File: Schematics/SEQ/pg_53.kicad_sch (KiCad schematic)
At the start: 6 parts, among them U5401 F30, U5402 F148, U5403 F02, U5404 F20, U5405 F240, U5406 F374

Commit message: Much SEQ polishing
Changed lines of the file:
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@@
   (bus (pts (xy 487.68 193.04) (xy 487.68 198.12) ) (stroke (width 0) (type solid) (color 0 0 0 0) ) )
   (bus (pts (xy 487.68 198.12) (xy 487.68 203.2) ) (stroke (width 0) (type solid) (color 0 0 0 0) ) )
-  (bus (pts (xy 487.68 203.2) (xy 487.68 210.82) ) (stroke (width 0) (type solid) (color 0 0 0 0) ) )
   (bus (pts (xy 487.68 93.98) (xy 487.68 99.06) ) (stroke (width 0) (type solid) (color 0 0 0 0) ) )
   (bus (pts (xy 487.68 93.98) (xy 497.84 93.98) ) (stroke (width 0) (type solid) (color 0 0 0 0) ) )

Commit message: KiCad 6
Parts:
- U5401: value F30 -> (none)
- U5402: value F148 -> (none)
- U5403: value F02 -> (none)
- U5404: value F20 -> (none)
- U5405: value F240 -> (none)
- U5406: value F374 -> (none)

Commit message: Recover from KiCad-6 munging
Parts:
- U5401: value (none) -> F30
- U5402: value (none) -> F148
- U5403: value (none) -> F02
- U5404: value (none) -> F20
- U5405: value (none) -> F240
- U5406: value (none) -> F374

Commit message: Megacompification
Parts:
- removed U5403: F02, symbol r1000:F02
- removed U5405: F240, symbol r1000:F240
- U5406: value F374 -> XREG14; symbol r1000:F374 -> r1000:XREG14; Location N17 -> x99; Name LMUAD1 -> LMUAD
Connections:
- net L_MACRO_HIC~: now also U5406.3 (OE); no longer U5406.1 (OE)
- net PD: now also U5406.16 (D5), U5406.20 (D7); no longer U5406.4 (D1)
- net PU: now also U5406.10 (D2), U5406.12 (D3), U5406.28 (D11), U5406.30 (D12), U5406.32 (D13), U5406.6 (D0), U5406.8 (D1); no longer U5406.17 (D6), U5406.3 (D0)
- net UADR~0: now also U5406.7 (Q0)
- net UADR~1: now also U5406.9 (Q1)
- net UADR~10: now also U5406.27 (Q10); no longer U5406.12 (Q4)
- net UADR~11: now also U5406.29 (Q11); no longer U5406.15 (Q5)
- net UADR~12: now also U5406.31 (Q12); no longer U5406.16 (Q6)
- net UADR~13: now also U5406.33 (Q13); no longer U5406.19 (Q7)
- net UADR~2: now also U5406.11 (Q2)
- net UADR~3: now also U5406.13 (Q3)
- net UADR~4: now also U5406.15 (Q4)
- net UADR~5: now also U5406.17 (Q5)
- net UADR~6: now also U5406.19 (Q6); no longer U5406.2 (Q0)
- net UADR~7: now also U5406.21 (Q7); no longer U5406.5 (Q1)
- net UADR~8: now also U5406.23 (Q8); no longer U5406.6 (Q2)
- net UADR~9: now also U5406.25 (Q9); no longer U5406.9 (Q3)
- net ~LOCAL.CLK~: now also U5406.1 (CLK); no longer U5406.11 (CLK)
- net at U5402.6 (Y0), U5404.1 (D0): now also U5406.22 (D8); no longer U5406.7 (D2)
- net at U5402.7 (Y1), U5404.2 (D1): now also U5406.24 (D9); no longer U5406.8 (D3)
- net at U5402.9 (Y2), U5404.4 (D2): now also U5406.26 (D10); no longer U5406.13 (D4)
- no-connect marks 4 -> 3

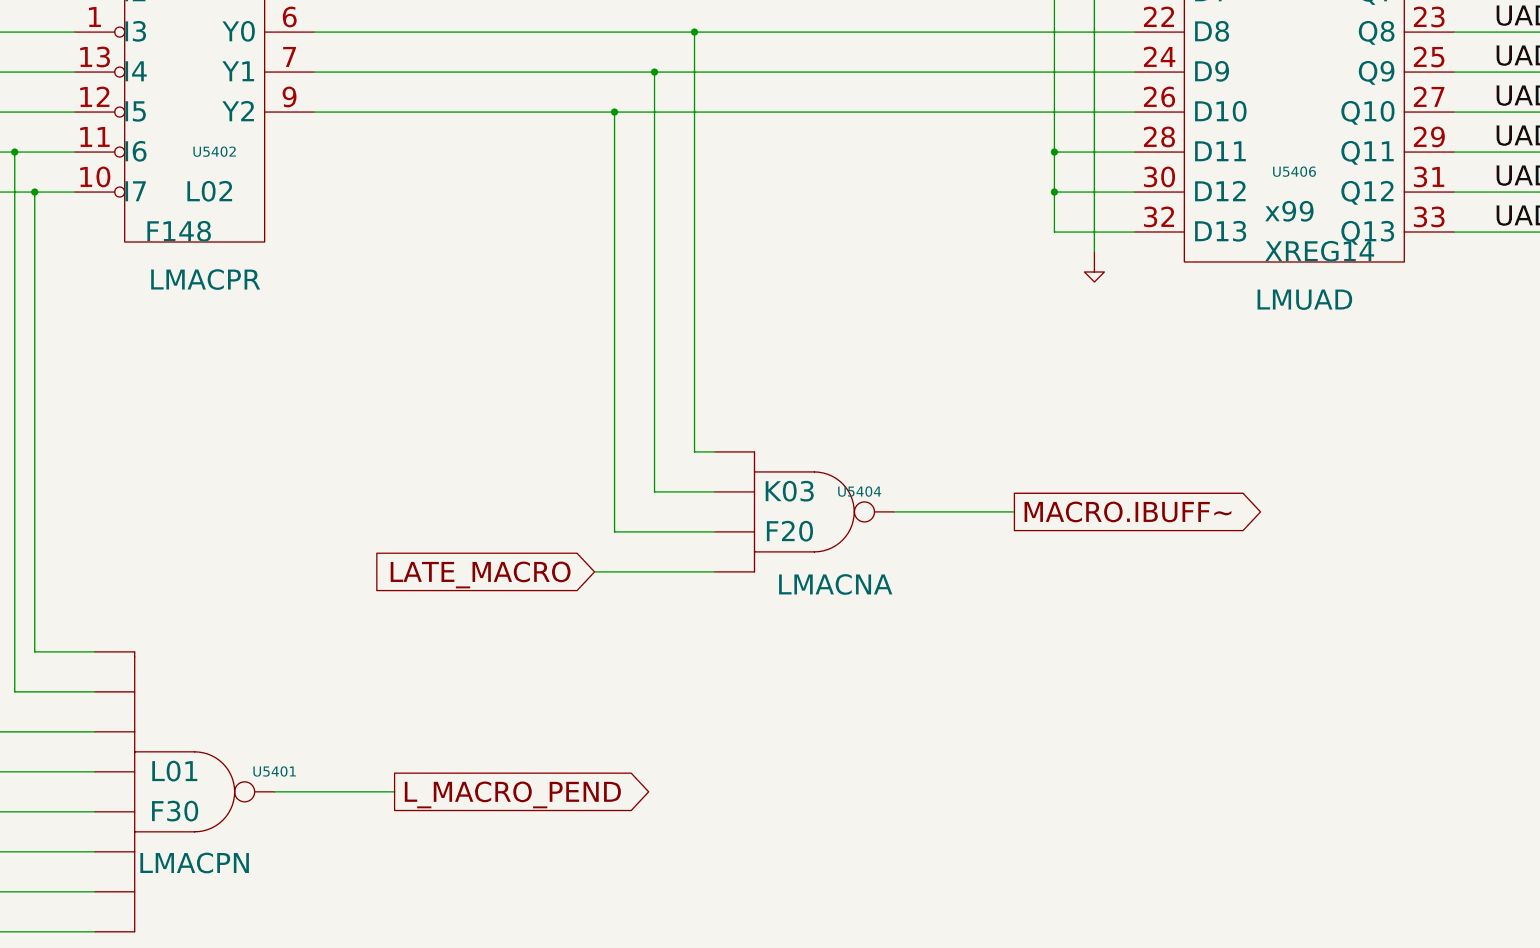
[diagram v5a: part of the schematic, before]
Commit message: Fix polarity of unused part of driven FIU bus.
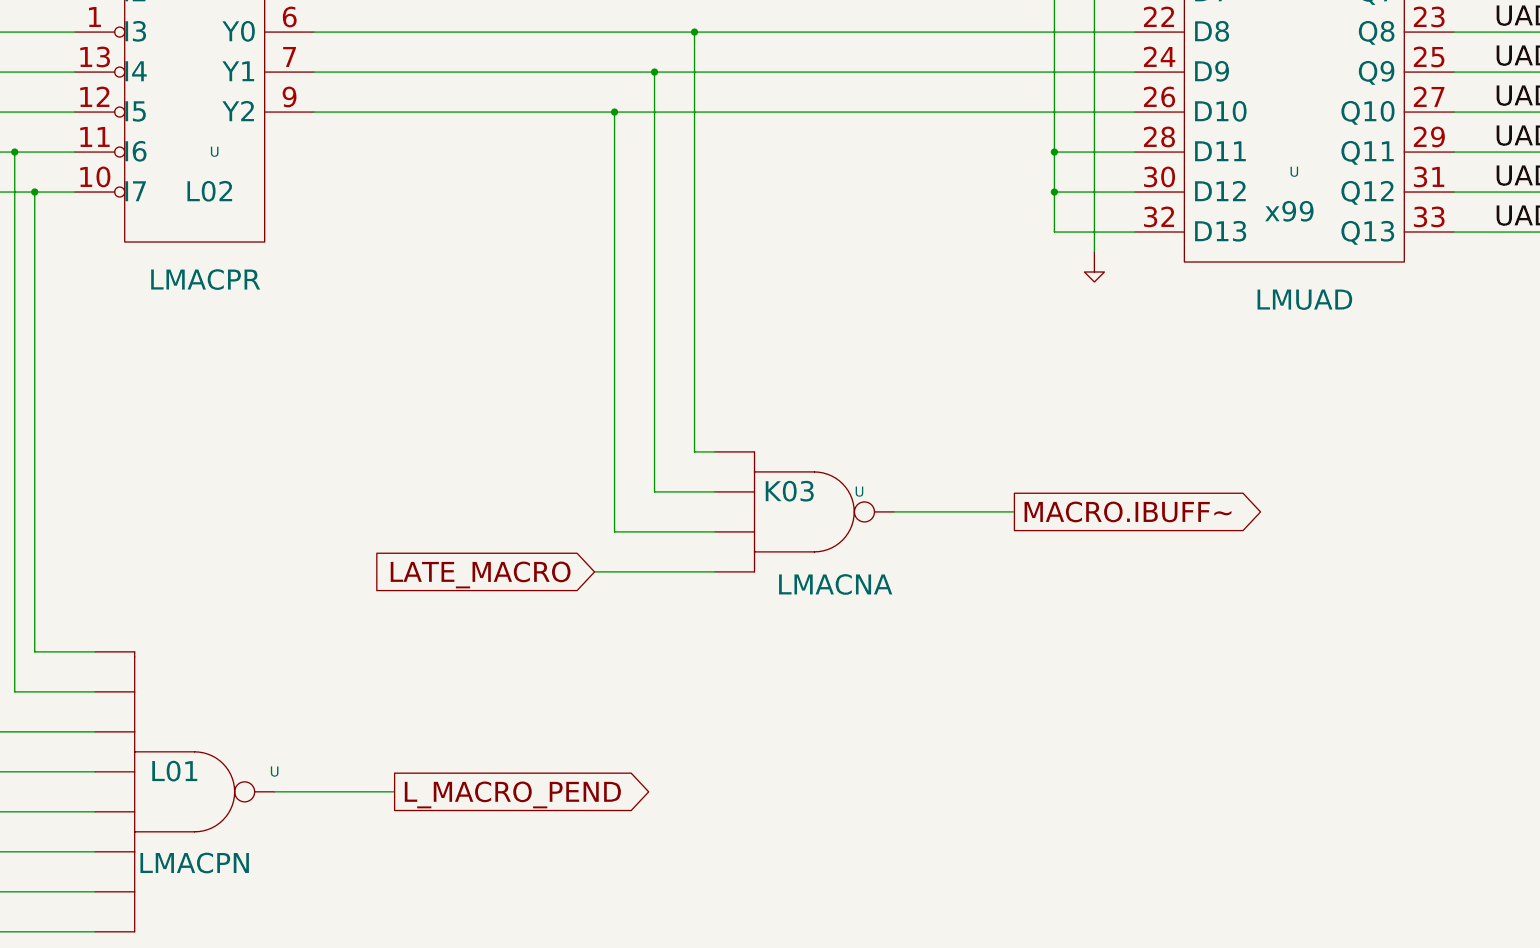
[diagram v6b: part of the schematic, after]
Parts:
- removed U5401: F30, symbol r1000:F30
- removed U5402: F148, symbol r1000:F148
- removed U5404: F20, symbol r1000:F20
- removed U5406: XREG14, symbol r1000:XREG14
- added U: (no value), symbol r1000:XREG14
- added U: (no value), symbol r1000:F20
- added U: (no value), symbol r1000:F148
- added U: (no value), symbol r1000:F30
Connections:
- net LATE_MACRO: now also U.5 (D3)
- net L_MACRO_HIC~: now also U.3 (OE)
- net L_MACRO_PEND: now also U.8 (Q)
- net MACRO.IBUFF~: now also U.6 (Q)
- net MAYBE_DISPATCH~: now also U.5 (E)
- net M_BRK_CLASS~: now also U.11 (I6), U.12 (D1)
- net M_IBUFF_MT~: now also U.10 (I7), U.11 (D0)
- net M_OVERFLOW~: now also U.3 (I1), U.5 (D6)
- net M_RES_REF~: now also U.1 (I3), U.3 (D4)
- net M_TOS_INVLD~: now also U.13 (I4), U.2 (D3)
- net M_UNDERFLOW~: now also U.4 (I0), U.6 (D7)
- net PD: now also U.16 (D5), U.20 (D7)
- net PU: now also U.1 (D2), U.10 (D2), U.12 (D3), U.12 (I5), U.14 (D4), U.18 (D6), U.28 (D11), U.30 (D12), U.32 (D13), U.6 (D0), U.8 (D1)
- net SEQ_STOP~: now also U.2 (I2), U.4 (D5)
- net UADR~0: now also U.7 (Q0)
- net UADR~1: now also U.9 (Q1)
- net UADR~10: now also U.27 (Q10)
- net UADR~11: now also U.29 (Q11)
- net UADR~12: now also U.31 (Q12)
- net UADR~13: now also U.33 (Q13)
- net UADR~2: now also U.11 (Q2)
- net UADR~3: now also U.13 (Q3)
- net UADR~4: now also U.15 (Q4)
- net UADR~5: now also U.17 (Q5)
- net UADR~6: now also U.19 (Q6)
- net UADR~7: now also U.21 (Q7)
- net UADR~8: now also U.23 (Q8)
- net UADR~9: now also U.25 (Q9)
- net ~LOCAL.CLK~: now also U.1 (CLK)
- new net: U.1 (D0), U.22 (D8), U.6 (Y0)
- new net: U.2 (D1), U.24 (D9), U.7 (Y1)
- new net: U.26 (D10), U.4 (D2), U.9 (Y2)
